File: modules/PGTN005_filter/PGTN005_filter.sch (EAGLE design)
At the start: 109 parts, among them IC1 TL084P, IC2 LM13700N, IC3 TL084P, IC4 TL082P, IC5 LM13700N, Q1 2N3904, Q2 2N3904, Q3 2N3906, Q4 2N3906

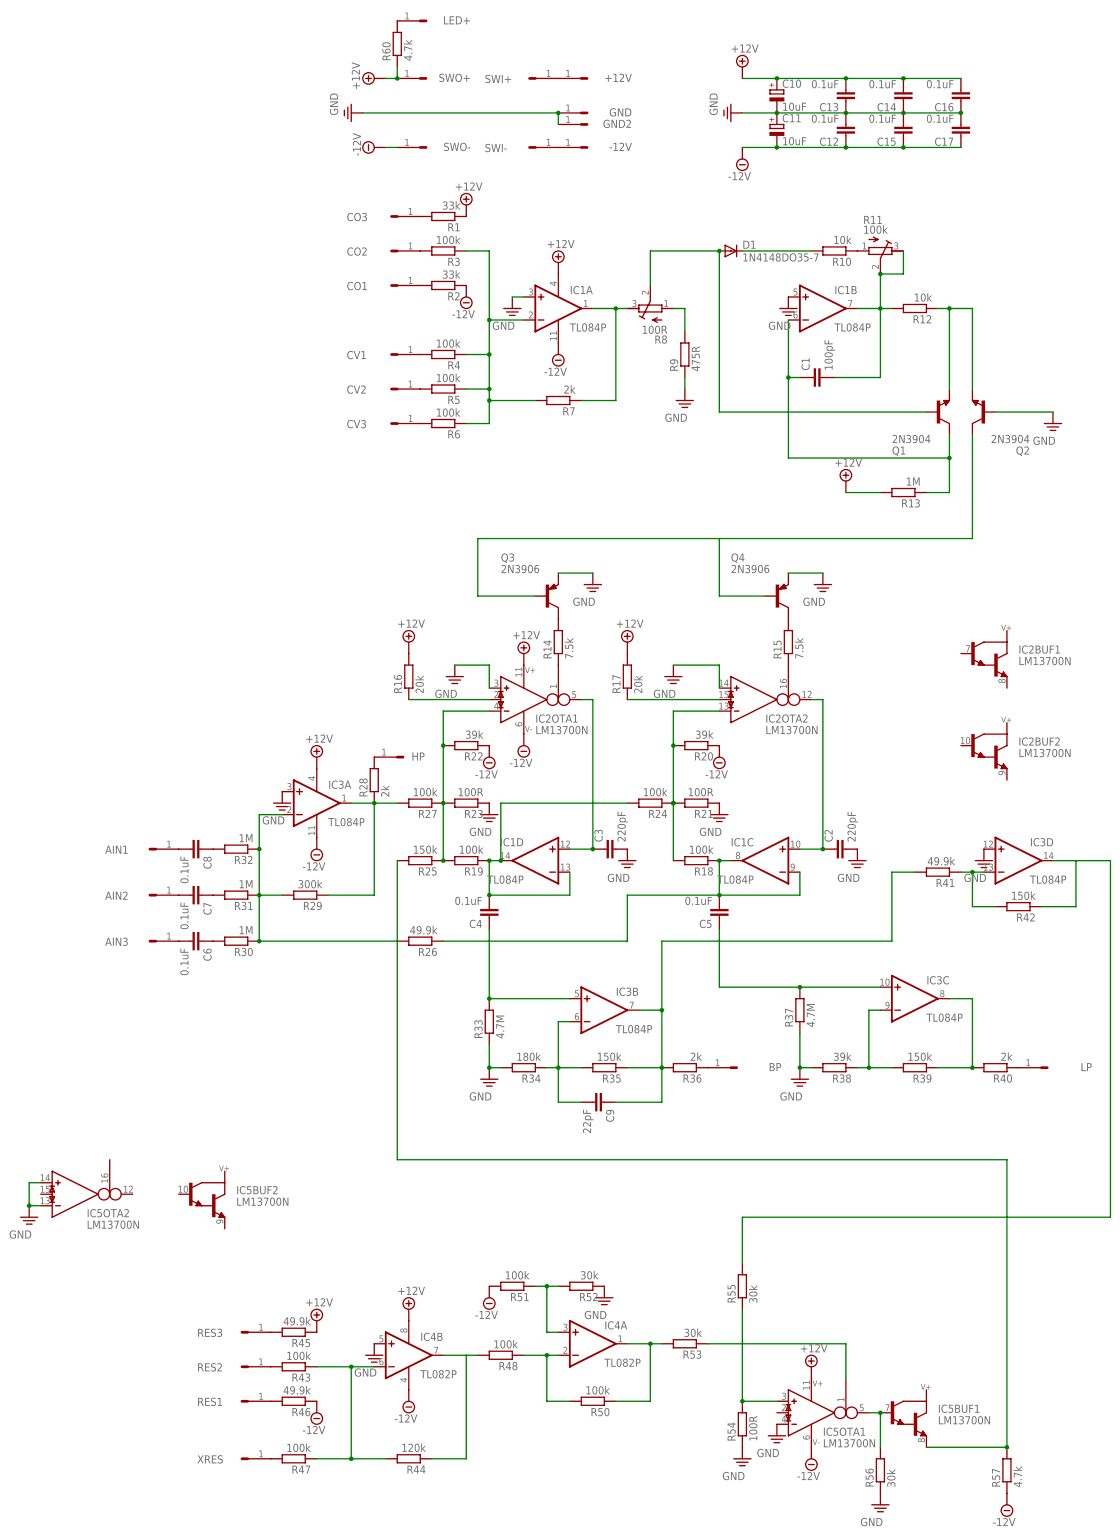
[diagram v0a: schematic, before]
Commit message: Changed 1M input resistors to 300k in filter to increase gain.
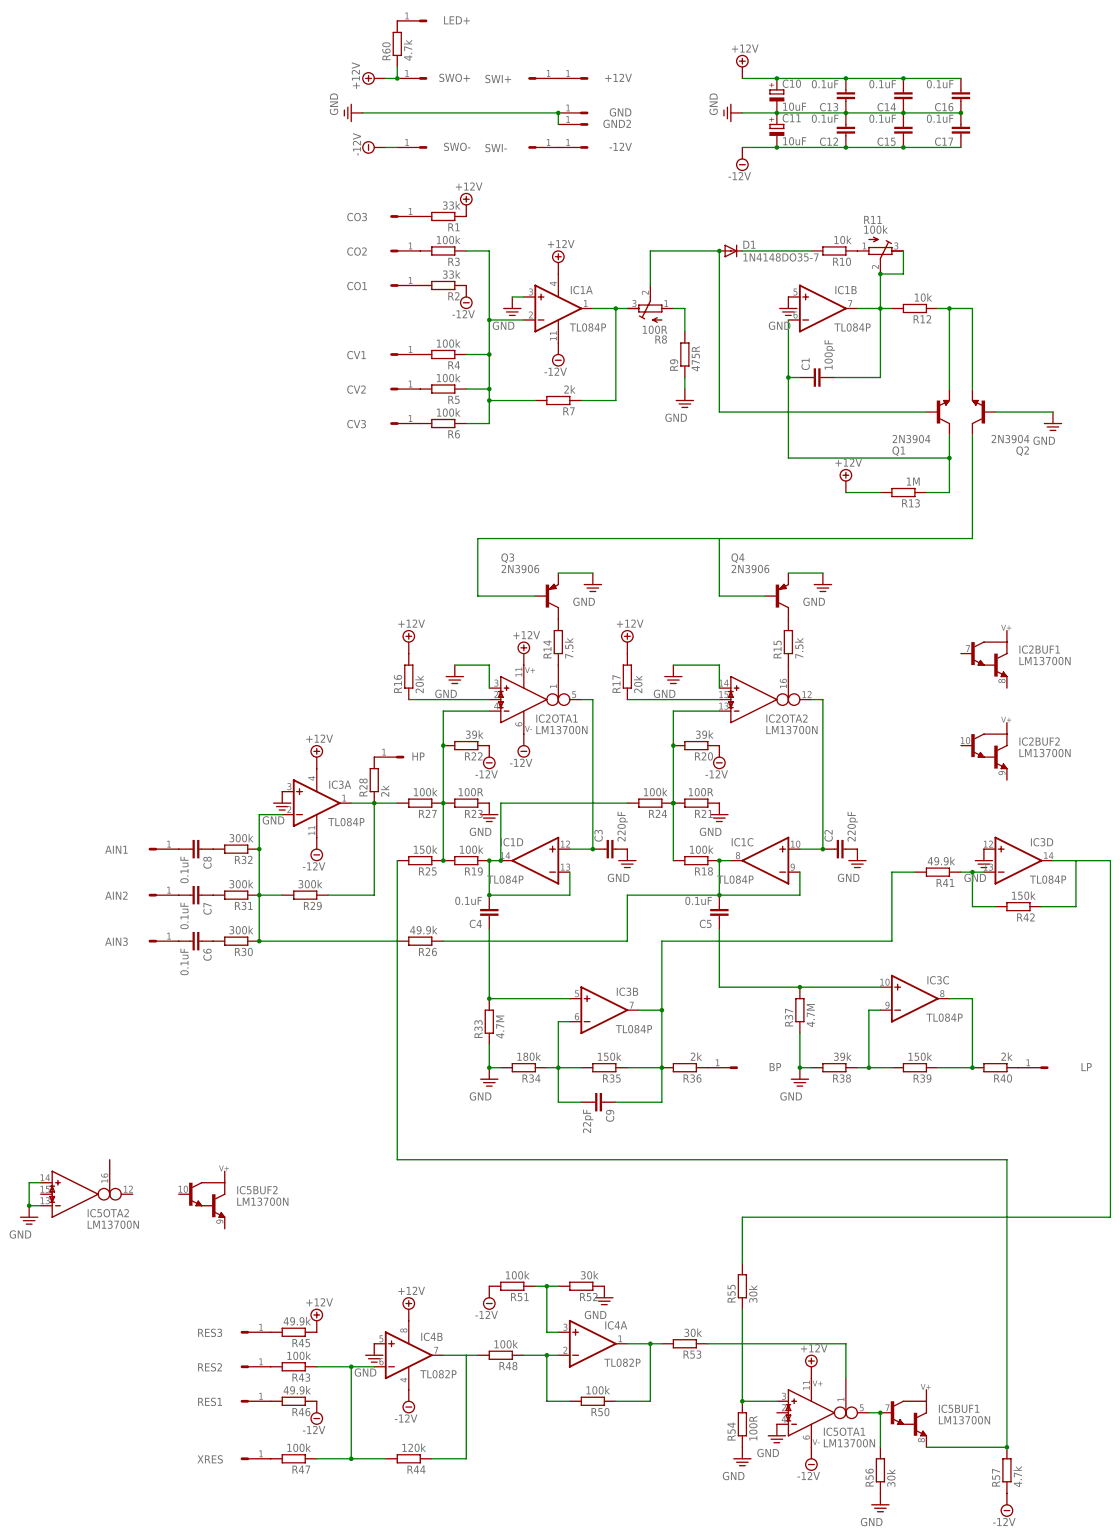
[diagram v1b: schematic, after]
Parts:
- R30, R31, R32: value 1M -> 300k
